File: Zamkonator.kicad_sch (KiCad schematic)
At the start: 31 parts, among them J1 Screw_Terminal_01x06, J2 Micro_SD_Card_Det1, J3 Conn_01x08_Male, J4 Screw_Terminal_01x06, J5 Conn_01x04_Female, J6 Conn_01x03_Female

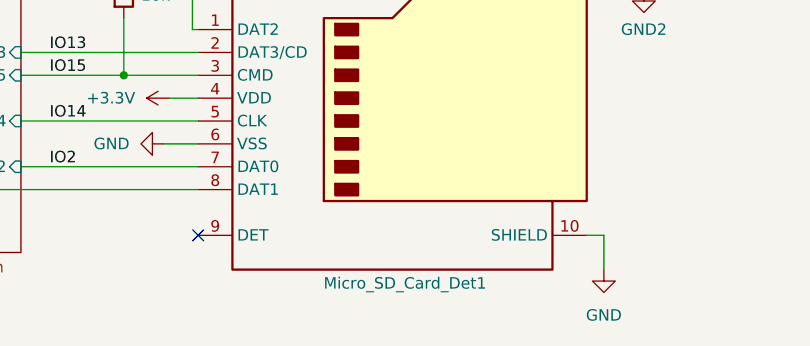
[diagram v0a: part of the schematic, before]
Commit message: Use cheaper SD card socket
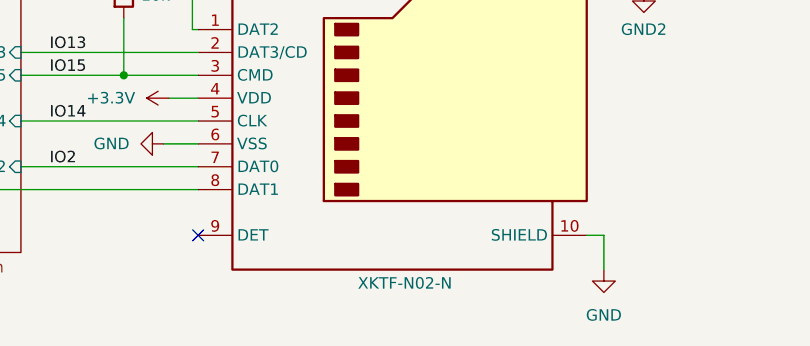
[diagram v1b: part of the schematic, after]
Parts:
- J2: value Micro_SD_Card_Det1 -> XKTF-N02-N; footprint Connector_Card:microSD_HC_Hirose_DM3AT-SF-PEJM5 -> project_footprints:TF-SMD_XKTF-N02-N; LCSC C114218 -> C381084
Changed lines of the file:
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@@
 			)
 		)
-		(property "Value" "Micro_SD_Card_Det1"
+		(property "Value" "XKTF-N02-N"
 			(at 240.792 160.274 0)
 			(effects
@@
 			)
 		)
-		(property "Footprint" "Connector_Card:microSD_HC_Hirose_DM3AT-SF-PEJM5"
+		(property "Footprint" "project_footprints:TF-SMD_XKTF-N02-N"
 			(at 292.735 124.46 0)
 			(effects
@@
 			)
 		)
-		(property "Datasheet" "https://www.lcsc.com/datasheet/lcsc_datasheet_1810301220_HRS-Hirose-DM3AT-SF-PEJM5_C114218.pdf"
+		(property "Datasheet" "https://www.lcsc.com/datasheet/C381084.pdf"
 			(at 240.665 139.7 0)
 			(effects
@@
 			)
 		)
-		(property "LCSC" "C114218"
+		(property "LCSC" "C381084"
 			(at 240.665 142.24 0)
 			(effects

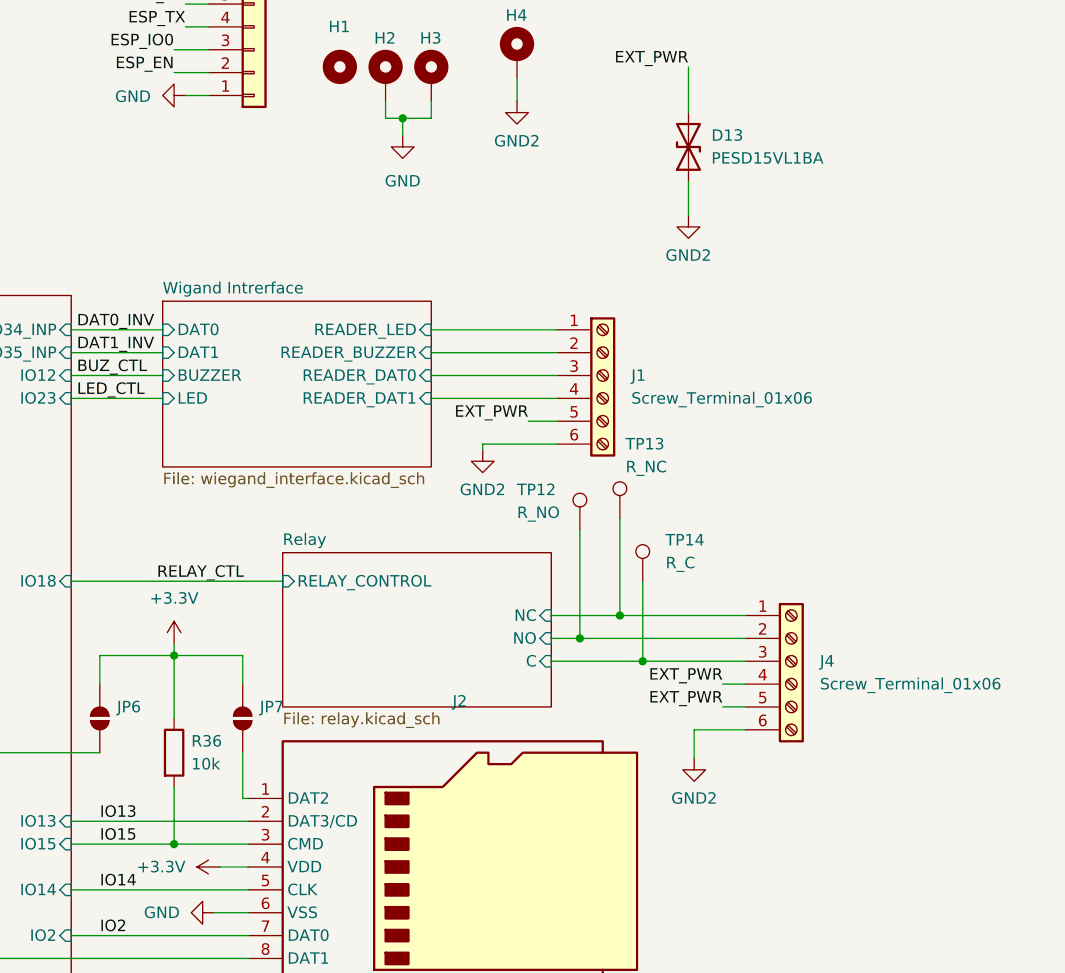
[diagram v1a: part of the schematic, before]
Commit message: Prepare push in connectors, add aux input
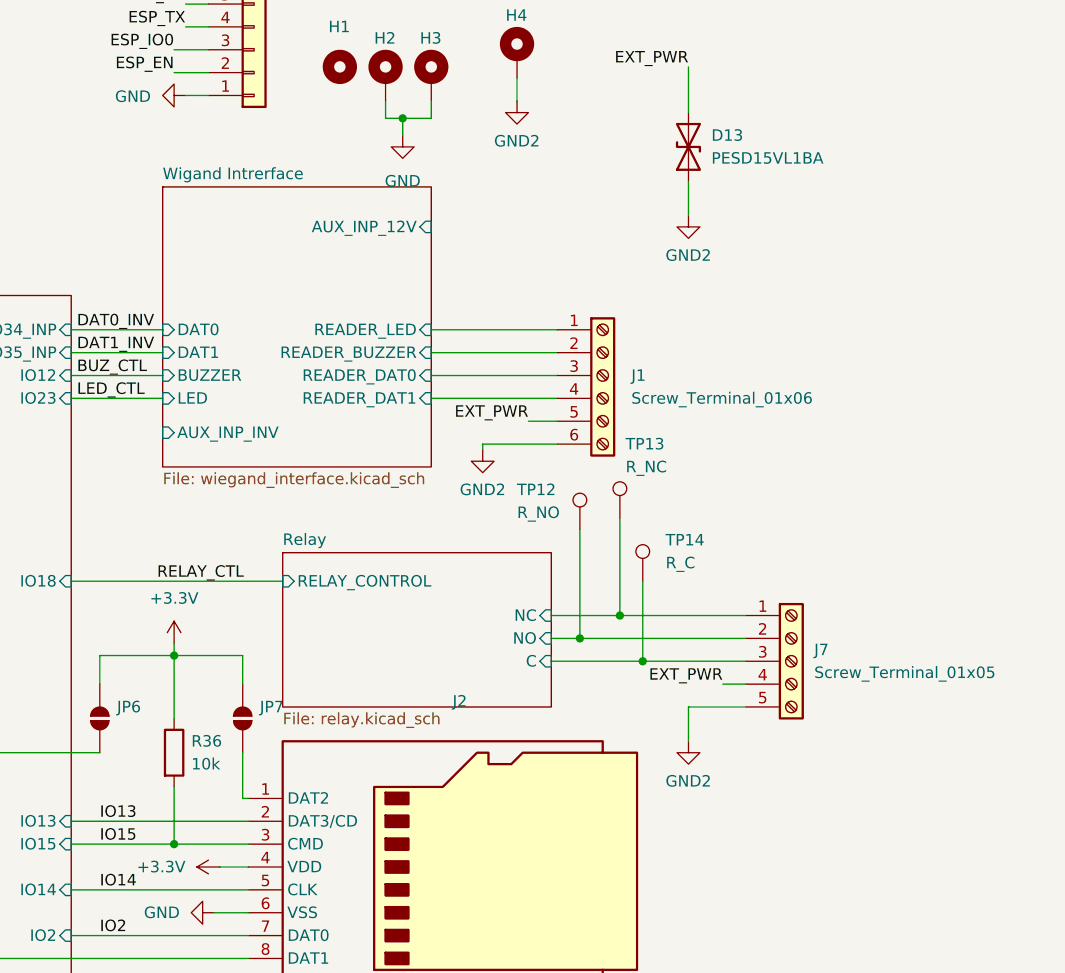
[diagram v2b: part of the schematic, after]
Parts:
- removed J4: Screw_Terminal_01x06, TerminalBlock_Phoenix:TerminalBlock_Phoenix_MPT-0,5-6-2.54_1x06_P2.54mm_Horizontal, symbol Connector:Screw_Terminal_01x06
- added J7: Screw_Terminal_01x05, project_footprints:CONN-TH_KF236-5.0-5P, symbol Connector:Screw_Terminal_01x05
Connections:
- net EXT_PWR: now also J7.4 (Pin_4)
- net GND2: now also J7.5 (Pin_5)
- net Relay/C: now also J7.3 (Pin_3)
- net Relay/NC: now also J7.1 (Pin_1)
- net Relay/NO: now also J7.2 (Pin_2)
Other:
- sheet Wigand Intrerface ports: added AUX_INP_12V, AUX_INP_INV; removed none
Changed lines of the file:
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@@
 	(wire
 		(pts
-			(xy 267.335 124.46) (xy 267.335 127.635)
+			(xy 266.7 121.92) (xy 266.7 125.73)
 		)
 		(stroke
@@
 	(wire
 		(pts
+			(xy 266.7 121.92) (xy 273.05 121.92)
+		)
+		(stroke
+			(width 0)
+			(type default)
+		)
+	)
+	(wire
+		(pts
 			(xy 198.12 80.01) (xy 208.28 80.01)
 		)
@@
 	(wire
 		(pts
-			(xy 267.335 124.46) (xy 273.05 124.46)
-		)
-		(stroke
-			(width 0)
-			(type default)
-		)
-	)
-	(wire
-		(pts
 			(xy 209.55 116.205) (xy 217.17 116.205)
 		)
@@
 	(wire
 		(pts
-			(xy 270.51 119.38) (xy 273.05 119.38)
-		)
-		(stroke
-			(width 0)
-			(type default)
-		)
-	)
-	(wire
-		(pts
 			(xy 198.12 107.95) (xy 221.615 107.95)
 		)
@@
 	(wire
 		(pts
-			(xy 270.51 121.92) (xy 273.05 121.92)
+			(xy 270.51 119.38) (xy 273.05 119.38)
 		)
 		(stroke
@@
 		)
 	)
-	(label "EXT_PWR"
-		(at 270.51 119.38 180)
-		(effects
-			(font
-				(size 1.27 1.27)
-			)
-			(justify right bottom)
-		)
-	)
 	(label "RT9400_VB1"
 		(at 75.565 40.64 270)
@@
 	)
 	(label "EXT_PWR"
-		(at 270.51 121.92 180)
+		(at 270.51 119.38 180)
 		(effects
 			(font
@@
 	)
 	(symbol
+		(lib_id "Connector:Screw_Terminal_01x05")
+		(at 278.13 116.84 0)
+		(unit 1)
+		(exclude_from_sim no)
+		(in_bom yes)
+		(on_board yes)
+		(dnp no)
+		(fields_autoplaced yes)
+		(property "Reference" "J7"
+			(at 280.67 115.5699 0)
+			(effects
+				(font
+					(size 1.27 1.27)
+				)
+				(justify left)
+			)
+		)
+		(property "Value" "Screw_Terminal_01x05"
+			(at 280.67 118.1099 0)
+			(effects
+				(font
+					(size 1.27 1.27)
+				)
+				(justify left)
+			)
+		)
+		(property "Footprint" "project_footprints:CONN-TH_KF236-5.0-5P"
+			(at 278.13 116.84 0)
+			(effects
+				(font
+					(size 1.27 1.27)
+				)
+				(hide yes)
+			)
+		)
+		(property "Datasheet" "~"
+			(at 278.13 116.84 0)
+			(effects
+				(font
+					(size 1.27 1.27)
+				)
+				(hide yes)
+			)
+		)
+		(property "Description" "Generic screw terminal, single row, 01x05, script generated (kicad-library-utils/schlib/autogen/connector/)"
+			(at 278.13 116.84 0)
+			(effects
+				(font
+					(size 1.27 1.27)
+				)
+				(hide yes)
+			)
+		)
+		(pin "4"
+		)
+		(pin "3"
+		)
+		(pin "2"
+		)
+		(pin "1"
+		)
+		(pin "5"
+		)
+		(instances
+			(project ""
+				(path "/727d6c0a-a0ef-4feb-9656-3db3cb90564a"
+					(reference "J7")
+					(unit 1)
+				)
+			)
+		)
+	)
+	(symbol
 		(lib_name "+12V_1")
 		(lib_id "power:+12V")
@@
 	(symbol
 		(lib_id "power:GND2")
-		(at 267.335 127.635 0)
+		(at 266.7 125.73 0)
 		(unit 1)
 		(exclude_from_sim no)
@@
 		(fields_autoplaced yes)
 		(property "Reference" "#PWR04"
-			(at 267.335 133.985 0)
+			(at 266.7 132.08 0)
 			(effects
 				(font
@@
 		)
 		(property "Value" "GND2"
-			(at 267.335 132.08 0)
+			(at 266.7 130.175 0)
 			(effects
 				(font
@@
 		)
 		(property "Footprint" ""
-			(at 267.335 127.635 0)
+			(at 266.7 125.73 0)
 			(effects
 				(font
@@
 		)
 		(property "Datasheet" ""
-			(at 267.335 127.635 0)
+			(at 266.7 125.73 0)
 			(effects
 				(font
@@
 		)
 		(property "Description" "Power symbol creates a global label with name \"GND2\" , ground"
-			(at 267.335 127.635 0)
+			(at 266.7 125.73 0)
 			(effects
 				(font
@@
 	)
 	(symbol
-		(lib_id "Connector:Screw_Terminal_01x06")
-		(at 278.13 116.84 0)
-		(unit 1)
-		(exclude_from_sim no)
-		(in_bom yes)
-		(on_board yes)
-		(dnp no)
-		(fields_autoplaced yes)
-		(property "Reference" "J4"
-			(at 281.305 116.8399 0)
-			(effects
-				(font
-					(size 1.27 1.27)
-				)
-				(justify left)
-			)
-		)
-		(property "Value" "Screw_Terminal_01x06"
-			(at 281.305 119.3799 0)
-			(effects
-				(font
-					(size 1.27 1.27)
-				)
-				(justify left)
-			)
-		)
-		(property "Footprint" "TerminalBlock_Phoenix:TerminalBlock_Phoenix_MPT-0,5-6-2.54_1x06_P2.54mm_Horizontal"
-			(at 278.13 116.84 0)
-			(effects
-				(font
-					(size 1.27 1.27)
-				)
-				(hide yes)
-			)
-		)
-		(property "Datasheet" "~"
-			(at 278.13 116.84 0)
-			(effects
-				(font
-					(size 1.27 1.27)
-				)
-				(hide yes)
-			)
-		)
-		(property "Description" ""
-			(at 278.13 116.84 0)
-			(effects
-				(font
-					(size 1.27 1.27)
-				)
-				(hide yes)
-			)
-		)
-		(pin "1"
-		)
-		(pin "2"
-		)
-		(pin "3"
-		)
-		(pin "4"
-		)
-		(pin "5"
-		)
-		(pin "6"
-		)
-		(instances
-			(project "Zamkonator"
-				(path "/727d6c0a-a0ef-4feb-9656-3db3cb90564a"
-					(reference "J4")
-					(unit 1)
-				)
-			)
-		)
-	)
-	(symbol
 		(lib_id "Connector:TestPoint")
 		(at 157.48 23.495 90)
@@
 	)
 	(sheet
-		(at 208.28 76.835)
-		(size 29.845 18.415)
+		(at 208.28 64.135)
+		(size 29.845 31.115)
 		(exclude_from_sim no)
 		(in_bom yes)
@@
 		)
 		(property "Sheetname" "Wigand Intrerface"
-			(at 208.28 76.1234 0)
+			(at 208.28 63.4234 0)
 			(effects
 				(font
@@
 			(effects
 				(font
+					(size 1.27 1.27)
+				)
+				(justify left)
+			)
+		)
+		(pin "AUX_INP_12V" input
+			(at 238.125 68.58 0)
+			(effects
+				(font
+					(size 1.27 1.27)
+				)
+				(justify right)
+			)
+		)
+		(pin "AUX_INP_INV" input
+			(at 208.28 91.44 180)
+			(effects
+				(font

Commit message: try playing around with the output screw terminals
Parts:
- removed J7: Screw_Terminal_01x05, project_footprints:CONN-TH_KF236-5.0-5P, symbol Connector:Screw_Terminal_01x05
- added J7: Screw_Terminal_01x07, project_footprints:CONN-TH_14P-P3.81_KF235-3.81-7P, symbol Connector:Screw_Terminal_01x07
- added J8: Screw_Terminal_01x02, project_footprints:CONN-TH_KF236-5.0-2P, symbol Connector:Screw_Terminal_01x02
- J1: footprint TerminalBlock_Phoenix:TerminalBlock_Phoenix_MPT-0,5-6-2.54_1x06_P2.54mm_Horizontal -> project_footprints:CONN-TH_KF236-5.0-6P
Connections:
- net EXT_PWR: now also J7.4 (Pin_4), J7.6 (Pin_6)
- net GND2: now also J7.5 (Pin_5), J7.7 (Pin_7), J8.2 (Pin_2)
- net Relay/C: now also J7.3 (Pin_3)
- net Relay/NC: now also J7.1 (Pin_1)
- net Relay/NO: now also J7.2 (Pin_2)
- new net Wigand Intrerface/AUX_INP_GND: J8.1 (Pin_1)
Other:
- sheet Wigand Intrerface ports: added AUX_INP_GND; removed none
- moved on the sheet: J1

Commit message: Finish the schematic maybe
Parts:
- removed J1: Screw_Terminal_01x06, project_footprints:CONN-TH_KF236-5.0-6P, symbol Connector:Screw_Terminal_01x06
- removed J7: Screw_Terminal_01x07, project_footprints:CONN-TH_14P-P3.81_KF235-3.81-7P, symbol Connector:Screw_Terminal_01x07
- removed JP6, JP7: SolderJumper_2_Open, Jumper:SolderJumper-2_P1.3mm_Open_RoundedPad1.0x1.5mm, symbol Jumper:SolderJumper_2_Open
- added C37, C38: 100n, Capacitor_SMD:C_0603_1608Metric_Pad1.08x0.95mm_HandSolder, symbol Device:C
- added D15: STATUS_LED_RED, LED_SMD:LED_0603_1608Metric, symbol Device:LED
- added D16: STATUS_LED_GREEN, LED_SMD:LED_0603_1608Metric, symbol Device:LED
- added J1: JST S8B-XH-A, Connector_JST:JST_XH_S8B-XH-A_1x08_P2.50mm_Horizontal, symbol Connector_Generic:Conn_01x08
- added J4: Com Jumper, Connector_PinHeader_2.54mm:PinHeader_1x03_P2.54mm_Vertical, symbol Connector:Conn_01x03_Pin
- added J7: WAGO 250-206, project_footprints:CONN-TH_250-206, symbol Connector:Screw_Terminal_01x06
- added J9: EXT_PWR_JUMPER, Connector_PinHeader_2.54mm:PinHeader_2x02_P2.54mm_Vertical, symbol Connector_Generic:Conn_02x02_Top_Bottom
- added R40, R41: 240, Resistor_SMD:R_0603_1608Metric_Pad0.98x0.95mm_HandSolder, symbol Device:R
- added U12: TCA9555RGER, Package_DFN_QFN:VQFN-24-1EP_4x4mm_P0.5mm_EP2.45x2.45mm, symbol Interface_Expansion:TCA9555RGER
- J8: value Screw_Terminal_01x02 -> WAGO 250-202; footprint project_footprints:CONN-TH_KF236-5.0-2P -> project_footprints:CONN-TH_250-202; LCSC C976596 -> C2765061
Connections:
- net +12V: now also J9.3 (Pin_3)
- net +3.3V: now also C37.1, C38.1, U12.21 (VCC)
- net AUX_INP_INV: now also U12.8 (P07)
- net BUZ_CTL: now also U12.15 (P15)
- net EXT_PWR: now also J1.3 (Pin_3), J4.1 (Pin_1), J7.6 (Pin_6), J9.1 (Pin_1)
- net GND: now also C37.2, C38.2, D15.1 (K), D16.1 (K), J9.4 (Pin_4), U12.18 (A0), U12.23 (A1), U12.24 (A2), U12.25 (EPAD), U12.9 (GND)
- net GND2: now also J1.1 (Pin_1), J4.3 (Pin_3), J7.4 (Pin_4), J7.5 (Pin_5), J9.2 (Pin_2)
- net LED_CTL: now also U12.16 (P16)
- net RELAY_CTL: now also U12.10 (P10)
- net SD_CARD_DETECT: now reaches J2.9 (DET)
- net SD_CARD_DETECT: now also U12.14 (P14)
- net IO13 renamed ESP32/IO13
- net IO14 renamed ESP32/IO14
- net IO15 renamed ESP32/IO15
- net IO2 renamed ESP32/IO2
- net Relay/C renamed R_C
- net R_C: now also J4.2 (Pin_2), J7.3 (Pin_3)
- net Relay/NC renamed R_NC
- net R_NC: now also J7.1 (Pin_1)
- net Relay/NO renamed R_NO
- net R_NO: now also J7.2 (Pin_2)
- net Wigand Intrerface/AUX_INP_GND renamed AUX_INP_GND
- new net: D16.2 (A), R41.1
- new net: D15.2 (A), R40.1
- new net I2C_INT: U12.22 (~{INT})
- new net READER_BUZZER: J1.5 (Pin_5)
- new net READER_DAT0: J1.2 (Pin_2)
- new net READER_DAT1: J1.4 (Pin_4)
- new net READER_LED: J1.6 (Pin_6)
- new net SCL: U12.19 (SCL)
- new net SDA: U12.20 (SDA)
- new net STATUS_LED_GREEN: R41.2, U12.5 (P04)
- new net STATUS_LED_RED: R40.2, U12.4 (P03)
- no-connect marks 3 -> 7
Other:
- note added: "https://phabricator.hskrk.pl/w/members/projekty/zamek/dokumentacja/"
- moved on the sheet: J2, J8, TP12, TP13, TP14

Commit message: Finish preliminary routing
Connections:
- net GND: no longer H3.1
- net GND2: now also H3.1
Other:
- sheet PoE PSU ports: added POE+_OUT, POE-_OUT; removed none
- moved on the sheet: H3
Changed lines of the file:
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@@
 	)
 	(junction
+		(at 247.65 53.34)
+		(diameter 0)
+		(color 0 0 0 0)
+	)
+	(junction
 		(at 137.16 81.28)
 		(diameter 0)
@@
 	)
 	(junction
-		(at 234.95 56.515)
-		(diameter 0)
-		(color 0 0 0 0)
-	)
-	(junction
 		(at 92.075 82.55)
 		(diameter 0)
@@
 	(wire
 		(pts
+			(xy 242.57 53.34) (xy 247.65 53.34)
+		)
+		(stroke
+			(width 0)
+			(type default)
+		)
+	)
+	(wire
+		(pts
 			(xy 241.3 68.58) (xy 251.46 68.58)
 		)
@@
 	(wire
 		(pts
+			(xy 242.57 52.07) (xy 242.57 53.34)
+		)
+		(stroke
+			(width 0)
+			(type default)
+		)
+	)
+	(wire
+		(pts
 			(xy 203.2 212.09) (xy 212.09 212.09)
 		)
@@
 	(wire
 		(pts
-			(xy 238.125 54.61) (xy 238.125 56.515)
-		)
-		(stroke
-			(width 0)
-			(type default)
-		)
-	)
-	(wire
-		(pts
 			(xy 135.89 154.94) (xy 139.7 154.94)
 		)
@@
 	(wire
 		(pts
-			(xy 234.95 56.515) (xy 238.125 56.515)
+			(xy 242.57 198.12) (xy 242.57 199.39)
 		)
 		(stroke
@@
 	(wire
 		(pts
-			(xy 242.57 198.12) (xy 242.57 199.39)
+			(xy 247.65 52.07) (xy 247.65 53.34)
 		)
 		(stroke
@@
 	(wire
 		(pts
-			(xy 247.65 52.07) (xy 247.65 54.61)
+			(xy 97.79 222.25) (xy 101.6 222.25)
 		)
 		(stroke
@@
 	(wire
 		(pts
-			(xy 97.79 222.25) (xy 101.6 222.25)
+			(xy 92.075 85.09) (xy 92.71 85.09)
 		)
 		(stroke
@@
 	(wire
 		(pts
-			(xy 92.075 85.09) (xy 92.71 85.09)
+			(xy 120.65 234.95) (xy 121.92 234.95)
 		)
 		(stroke
@@
 	(wire
 		(pts
-			(xy 120.65 234.95) (xy 121.92 234.95)
+			(xy 97.79 231.14) (xy 97.79 227.33)
 		)
 		(stroke
@@
 	(wire
 		(pts
-			(xy 97.79 231.14) (xy 97.79 227.33)
+			(xy 209.55 48.895) (xy 213.36 48.895)
 		)
 		(stroke
@@
 	(wire
 		(pts
-			(xy 209.55 48.895) (xy 213.36 48.895)
+			(xy 80.01 74.93) (xy 80.01 76.2)
 		)
 		(stroke
@@
 	(wire
 		(pts
+			(xy 247.65 53.34) (xy 247.65 54.61)
+		)
+		(stroke
+			(width 0)
+			(type default)
+		)
+	)
+	(wire
+		(pts
 			(xy 158.115 26.035) (xy 157.48 26.035)
 		)
@@
 	(wire
 		(pts
+			(xy 77.47 74.93) (xy 77.47 76.2)
+		)
+		(stroke
+			(width 0)
+			(type default)
+		)
+	)
+	(wire
+		(pts
 			(xy 113.03 39.37) (xy 113.03 44.45)
 		)
@@
 		)
 	)
-	(label "RT9400_VB2"
-		(at 92.075 86.36 270)
-		(effects
-			(font
-				(size 1.27 1.27)
-			)
-			(justify right bottom)
-		)
-	)
 	(label "CLK_EN"
 		(at 199.39 34.925 180)
@@
 		)
 	)
-	(label "RT9400_VB1"
-		(at 92.075 81.28 90)
-		(effects
-			(font
-				(size 1.27 1.27)
-			)
-			(justify left bottom)
-		)
-	)
 	(label "I2C_INT"
 		(at 99.06 191.77 180)
@@
 		)
 	)
+	(label "RT9400_VB2"
+		(at 80.01 74.93 90)
+		(effects
+			(font
+				(size 1.27 1.27)
+			)
+			(justify left bottom)
+		)
+	)
 	(label "EMAC_MDC"
 		(at 135.89 109.22 0)
@@
 		)
 	)
+	(label "RT9400_VB1"
+		(at 77.47 74.93 90)
+		(effects
+			(font
+				(size 1.27 1.27)
+			)
+			(justify left bottom)
+		)
+	)
 	(label "ESP_EN"
 		(at 174.625 73.025 90)
@@
 	(symbol
 		(lib_id "Mechanical:MountingHole_Pad")
-		(at 238.125 52.07 0)
+		(at 242.57 49.53 0)
 		(unit 1)
 		(exclude_from_sim no)
@@
 		(dnp no)
 		(property "Reference" "H3"
-			(at 236.855 47.625 0)
+			(at 241.3 45.085 0)
 			(effects
 				(font
@@
 		)
 		(property "Value" "MountingHole_Pad"
-			(at 234.95 43.815 0)
+			(at 239.395 41.275 0)
 			(effects
 				(font
@@
 		)
 		(property "Footprint" "MountingHole:MountingHole_3.2mm_M3_Pad_Via"
-			(at 238.125 52.07 0)
+			(at 242.57 49.53 0)
 			(effects
 				(font
@@
 		)
 		(property "Datasheet" "~"
-			(at 238.125 52.07 0)
+			(at 242.57 49.53 0)
 			(effects
 				(font
@@
 		)
 		(property "Description" ""
-			(at 238.125 52.07 0)
+			(at 242.57 49.53 0)
 			(effects
 				(font
@@
 			(effects
 				(font
+					(size 1.27 1.27)
+				)
+				(justify right)
+			)
+		)
+		(pin "POE+_OUT" input
+			(at 77.47 76.2 90)
+			(effects
+				(font
+					(size 1.27 1.27)
+				)
+				(justify right)
+			)
+		)
+		(pin "POE-_OUT" input
+			(at 80.01 76.2 90)
+			(effects
+				(font

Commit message: Finish routing
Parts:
- removed H2: MountingHole_Pad, MountingHole:MountingHole_3.2mm_M3_Pad_Via, symbol Mechanical:MountingHole_Pad
- added D17: 1N4007, Diode_SMD:D_SMA_Handsoldering, symbol Diode:1N4007
- added H2: MountingHole_Pad, MountingHole:MountingHole_3.2mm_M3, symbol Mechanical:MountingHole
- added R28, R30: 4.7k, Resistor_SMD:R_0603_1608Metric_Pad0.98x0.95mm_HandSolder, symbol Device:R
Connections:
- net +3.3V: now also R28.1, R30.1
- net EXT_PWR: now also D17.1 (K)
- net GND2: now also D17.2 (A)
- net SCL: now also R28.2
- net SDA: now also R30.2

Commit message: BOM updates
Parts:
- D17: LCSC (none) -> C7528875
- H3, H4, TP12, TP13, TP14: now left out of the parts list
- J3: LCSC (none) -> C37208
- J4: LCSC (none) -> C2937625
- J5: LCSC (none) -> C2718488
- J6: LCSC (none) -> C7509516
- J7: LCSC C2765065 -> C7470120
- J8: LCSC C2765061 -> C5443567
- J9: LCSC (none) -> C7501273
- R34, R35: now not fitted
- U12: LCSC (none) -> C42420609

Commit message: misc updates, extend board
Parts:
- added J10, J11: WAGO 250-202, project_footprints:CONN-TH_250-202, symbol Connector:Screw_Terminal_01x02
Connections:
- net GND2: now also J10.2 (Pin_2), J11.2 (Pin_2)
- net AUX_INP3_INV: now reaches U12.6 (P05)
- net AUX_INP2_INV: now reaches U12.7 (P06)
- net AUX_INP_GND renamed AUX_INP1_GND
- net AUX_INP_INV renamed AUX_INP1_INV
- new net AUX_INP2_GND: J10.1 (Pin_1)
- new net AUX_INP3_GND: J11.1 (Pin_1)
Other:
- sheet Wigand Intrerface ports: added AUX_INP1_GND, AUX_INP1_INV, AUX_INP2_GND, AUX_INP2_INV, AUX_INP3_GND, AUX_INP3_INV; removed AUX_INP_GND, AUX_INP_INV
- moved on the sheet: D13
